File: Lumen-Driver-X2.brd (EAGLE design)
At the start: 60 x 55 mm, 30 parts, among them J1 AVR_SPI_PRG_6PTH, U1 Tiny45-20-SMT, Y1 8Mhz

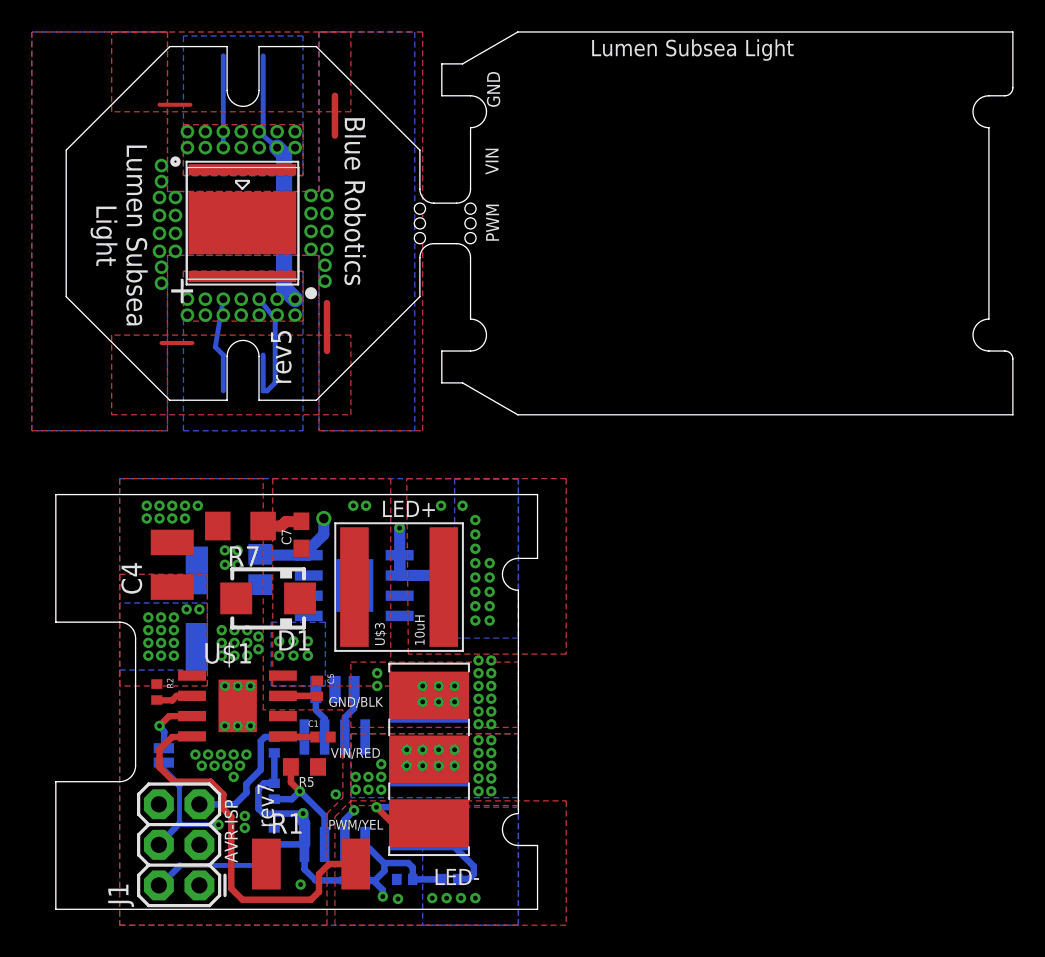
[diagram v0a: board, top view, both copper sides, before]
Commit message: Updated R2 design. Ordered and tested.
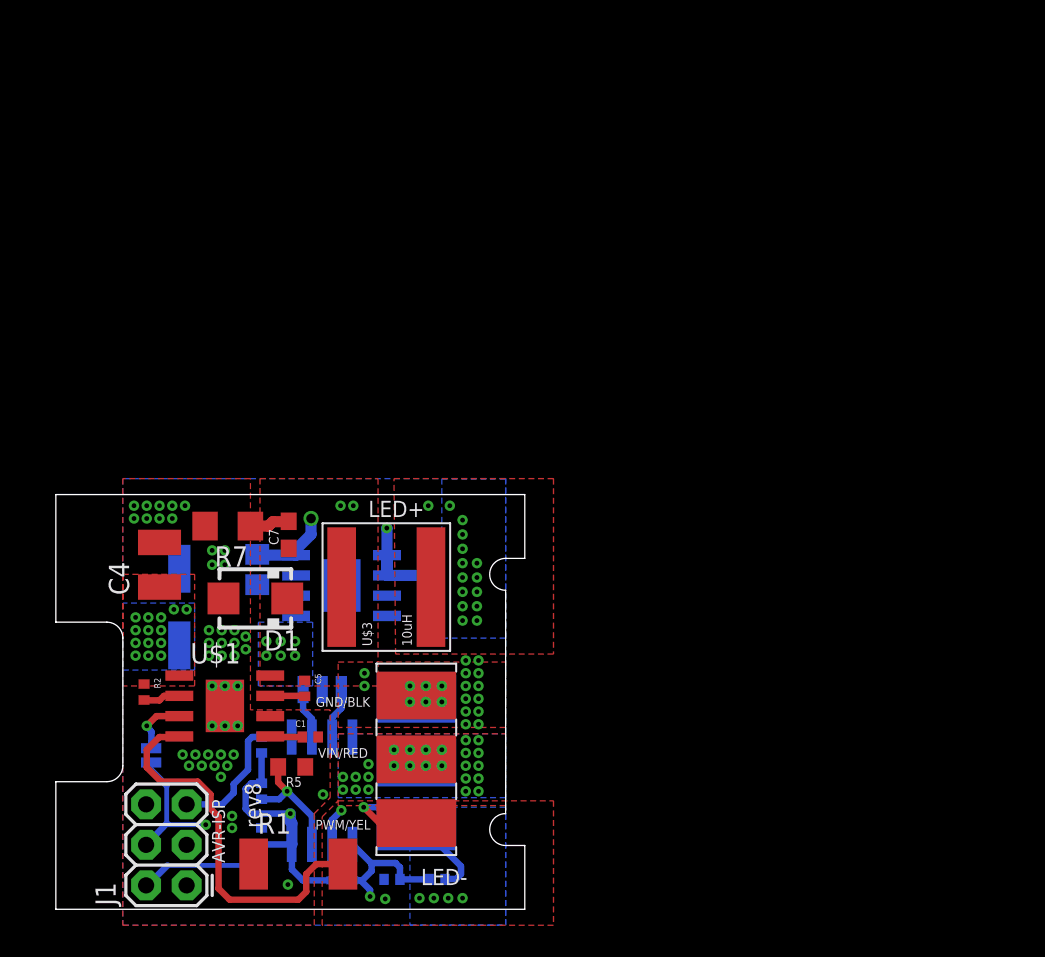
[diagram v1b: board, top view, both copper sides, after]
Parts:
- removed C2: 0.68uF 100V, resistor:C0805
- removed U$10: LOGOBR-LOGO-MS-COPPER, BlueRobotics-Main:BR-LOGO-MEDIUM-SMALL-COPPER
- removed U$2: LED-MK-R, BlueRobotics-Main:MK-R
- moved C3 1.10 mm to (7.74, 18.9)
- moved C1 0.80 mm to (15.9, 10.8)
- moved C7 0.80 mm to (14.6, 23.5)
- moved D1 0.80 mm to (12.5, 19.5)
- moved J1 0.80 mm to (8.20, 1.50)
- moved R1 0.80 mm to (15.2, 2.83)
- moved R5 0.80 mm to (14.8, 8.93)
- moved R6 0.80 mm to (23.9, 1.88)
- moved R8 0.80 mm to (21.1, 1.88)
- moved SJ1 0.80 mm to (5.97, 9.65)
- moved U$1 0.80 mm to (10.6, 12.8)
- moved U$13 0.80 mm to (17.9, 20.3)
- moved U$3 0.80 mm to (20.7, 20.2)
- moved C4 0.80 mm to (6.50, 21.6)
- moved R2 0.80 mm to (5.53, 13.6)
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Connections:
- removed net EXT: U$2.EXP
- removed net LED+ISO: C2.2, U$2.A
- removed net LED-ISO: C2.1, U$2.C
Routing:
- net LED-ISO: track 18.9 -> 0.00 mm, vias 14 -> 0
- net LED+ISO: track 15.8 -> 0.00 mm, vias 14 -> 0
- net EXT: track 9.38 -> 0.00 mm, vias 22 -> 0
- net VIN: track 7.15 -> 6.53 mm
- removed copper zone on layer 1, net EXT
- removed copper zone on layer 15, net EXT
- removed copper zone on layer 16, net EXT
- removed copper zone on layer 2, net EXT
- removed copper zone on layer 1, net LED+ISO
- removed copper zone on layer 16, net LED+ISO
- removed copper zone on layer 1, net LED-ISO
- removed copper zone on layer 16, net LED-ISO
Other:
- board size 60 x 55 mm -> 29.4 x 26 mm
- board text added: "rev8"
- board text removed: "+"
- board text removed: "Blue Robotics"
- board text removed: "BlueRobotics"
- board text removed: "Daisy chain pads"
- board text removed: "GND"
- board text removed: "Lumen Subsea Light"
- board text removed: "PWM"
- board text removed: "VIN"
- board text removed: "rev5"
- board text removed: "rev7"
